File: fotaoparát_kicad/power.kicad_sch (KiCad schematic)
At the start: 59 parts, among them J2 Conn_01x12_Pin, J3 Conn_01x12_Pin

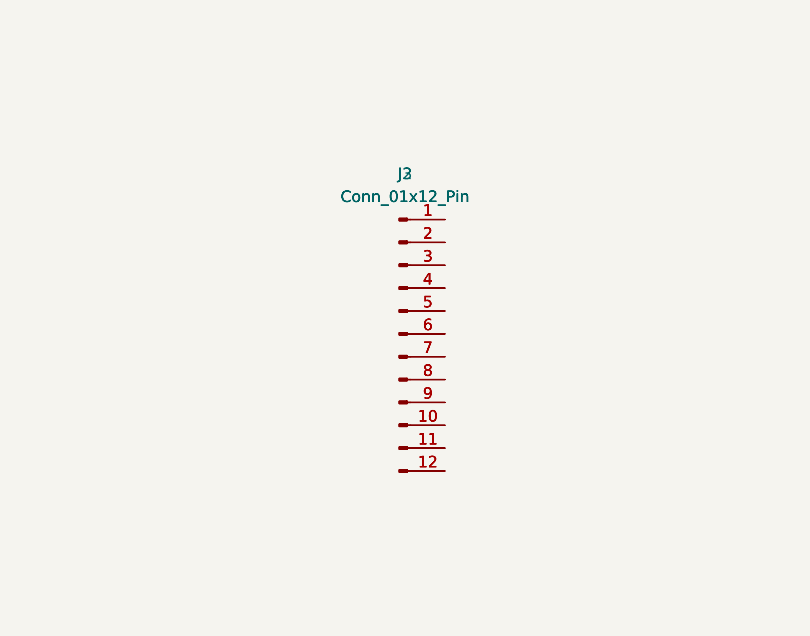
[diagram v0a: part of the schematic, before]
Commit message: Udelal jsem pullupy na tlacitka z fotaku
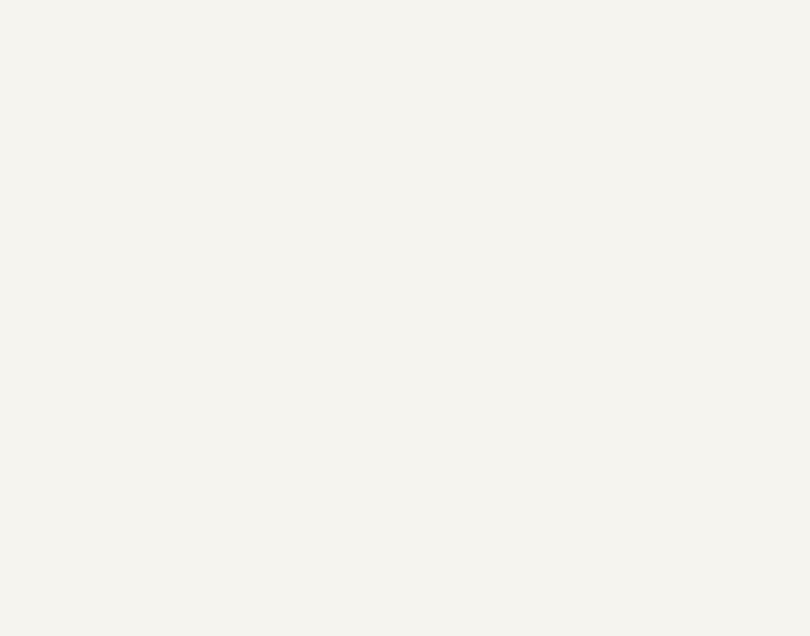
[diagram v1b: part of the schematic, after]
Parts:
- removed J2: Conn_01x12_Pin, Connector_FFC-FPC:Hirose_FH12-11S-0.5SH_1x11-1MP_P0.50mm_Horizontal, symbol Connector:Conn_01x12_Pin
- removed J3: Conn_01x12_Pin, symbol Connector:Conn_01x12_Pin
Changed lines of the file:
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@@
-	)
-	(symbol
-		(lib_id "Connector:Conn_01x12_Pin")
-		(at 334.01 67.31 0)
-		(unit 1)
-		(exclude_from_sim no)
-		(in_bom yes)
-		(on_board yes)
-		(dnp no)
-		(fields_autoplaced yes)
-		(property "Reference" "J3"
-			(at 334.645 49.53 0)
-			(effects
-				(font
-					(size 1.27 1.27)
-				)
-			)
-		)
-		(property "Value" "Conn_01x12_Pin"
-			(at 334.645 52.07 0)
-			(effects
-				(font
-					(size 1.27 1.27)
-				)
-			)
-		)
-		(property "Footprint" ""
-			(at 334.01 67.31 0)
-			(effects
-				(font
-					(size 1.27 1.27)
-				)
-				(hide yes)
-			)
-		)
-		(property "Datasheet" "~"
-			(at 334.01 67.31 0)
-			(effects
-				(font
-					(size 1.27 1.27)
-				)
-				(hide yes)
-			)
-		)
-		(property "Description" "Generic connector, single row, 01x12, script generated"
-			(at 334.01 67.31 0)
-			(effects
-				(font
-					(size 1.27 1.27)
-				)
-				(hide yes)
-			)
-		)
-		(pin "7"
-		)
-		(pin "4"
-		)
-		(pin "2"
-		)
-		(pin "12"
-		)
-		(pin "11"
-		)
-		(pin "3"
-		)
-		(pin "1"
-		)
-		(pin "6"
-		)
-		(pin "9"
-		)
-		(pin "10"
-		)
-		(pin "8"
-		)
-		(pin "5"
-		)
-		(instances
-			(project ""
-				(path "/0ab33720-0b6a-449c-80c0-2b7abe4d9450/04ebdae2-67d7-4749-bd3e-f9c05089f6fb"
-					(reference "J3")
-					(unit 1)
-				)
-			)
-		)
 	)
 	(symbol
@@
 					(unit 1)
 				)
-			)
-		)
-	)
-	(symbol
-		(lib_id "Connector:Conn_01x12_Pin")
-		(at 334.01 67.31 0)
-		(unit 1)
-		(exclude_from_sim no)
-		(in_bom yes)
-		(on_board yes)
-		(dnp no)
-		(fields_autoplaced yes)
-		(property "Reference" "J2"
-			(at 334.645 49.53 0)
-			(effects
-				(font
-					(size 1.27 1.27)
-				)
-			)
-		)
-		(property "Value" "Conn_01x12_Pin"
-			(at 334.645 52.07 0)
-			(effects
-				(font
-					(size 1.27 1.27)
-				)
-			)
-		)
-		(property "Footprint" "Connector_FFC-FPC:Hirose_FH12-11S-0.5SH_1x11-1MP_P0.50mm_Horizontal"
-			(at 334.01 67.31 0)
-			(effects
-				(font
-					(size 1.27 1.27)
-				)
-				(hide yes)
-			)
-		)
-		(property "Datasheet" "~"
-			(at 334.01 67.31 0)
-			(effects
-				(font
-					(size 1.27 1.27)
-				)
-				(hide yes)
-			)
-		)
-		(property "Description" "Generic connector, single row, 01x12, script generated"
-			(at 334.01 67.31 0)
-			(effects
-				(font
-					(size 1.27 1.27)
-				)
-				(hide yes)
-			)
-		)
-		(pin "7"
-		)
-		(pin "4"
-		)
-		(pin "2"
-		)
-		(pin "12"
-		)
-		(pin "11"
-		)
-		(pin "3"
-		)
-		(pin "1"
-		)
-		(pin "6"
-		)
-		(pin "9"
-		)
-		(pin "10"
-		)
-		(pin "8"
-		)
-		(pin "5"
-		)
-		(instances
-			(project ""
-				(path "/0ab33720-0b6a-449c-80c0-2b7abe4d9450/04ebdae2-67d7-4749-bd3e-f9c05089f6fb"
-					(reference "J2")
-					(unit 1)
-				)
